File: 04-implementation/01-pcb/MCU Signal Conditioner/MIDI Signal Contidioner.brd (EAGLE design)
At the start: 78 x 31.5 mm, 26 parts, among them J2 ARDUINO-CONN-8X2, J3 ARDUINO-CONN-8X2, U4 24CS01, U6 MCP1700-SOT89, X1 SSW-107-02-S-D, X2 SSW-107-02-S-D, X3 SSW-107-02-S-D, X4 SSW-107-02-S-D, X5 MINI-USB-SHIELD-32005-201

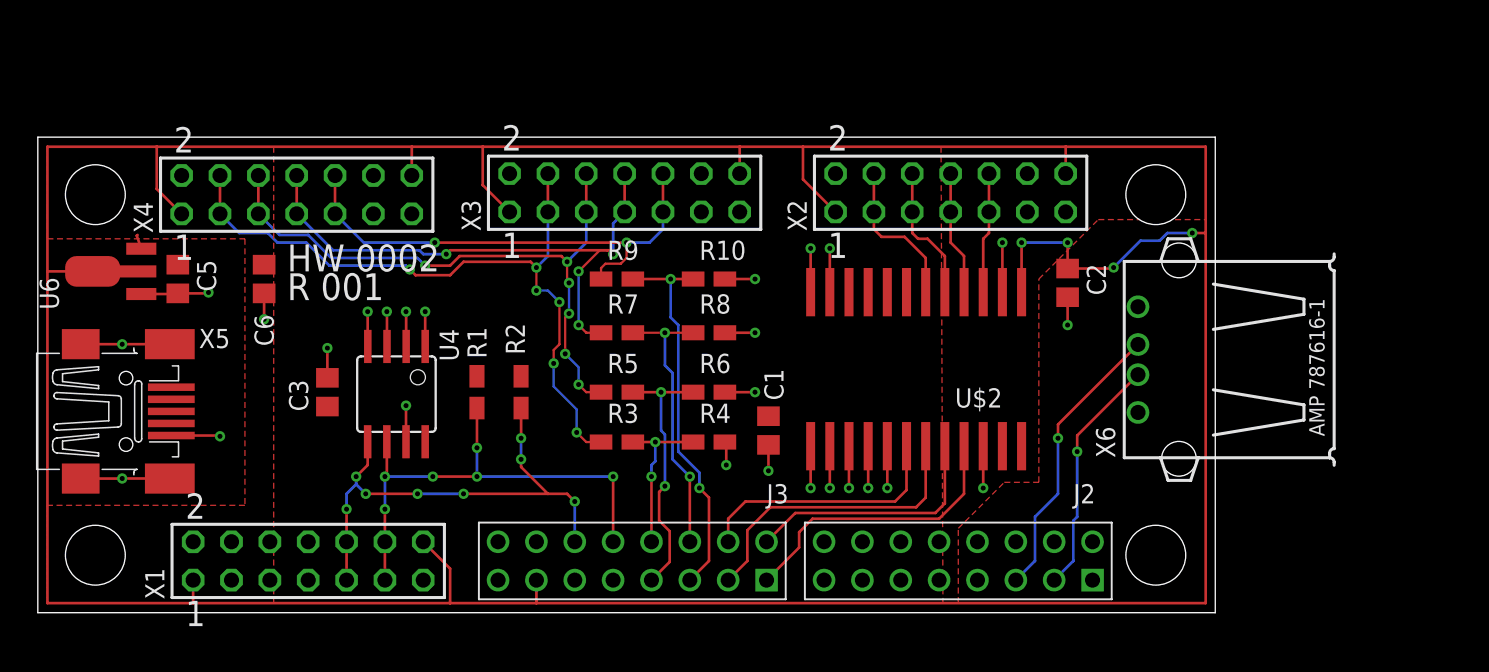
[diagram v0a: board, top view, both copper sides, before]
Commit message: Add files for PCB releases.
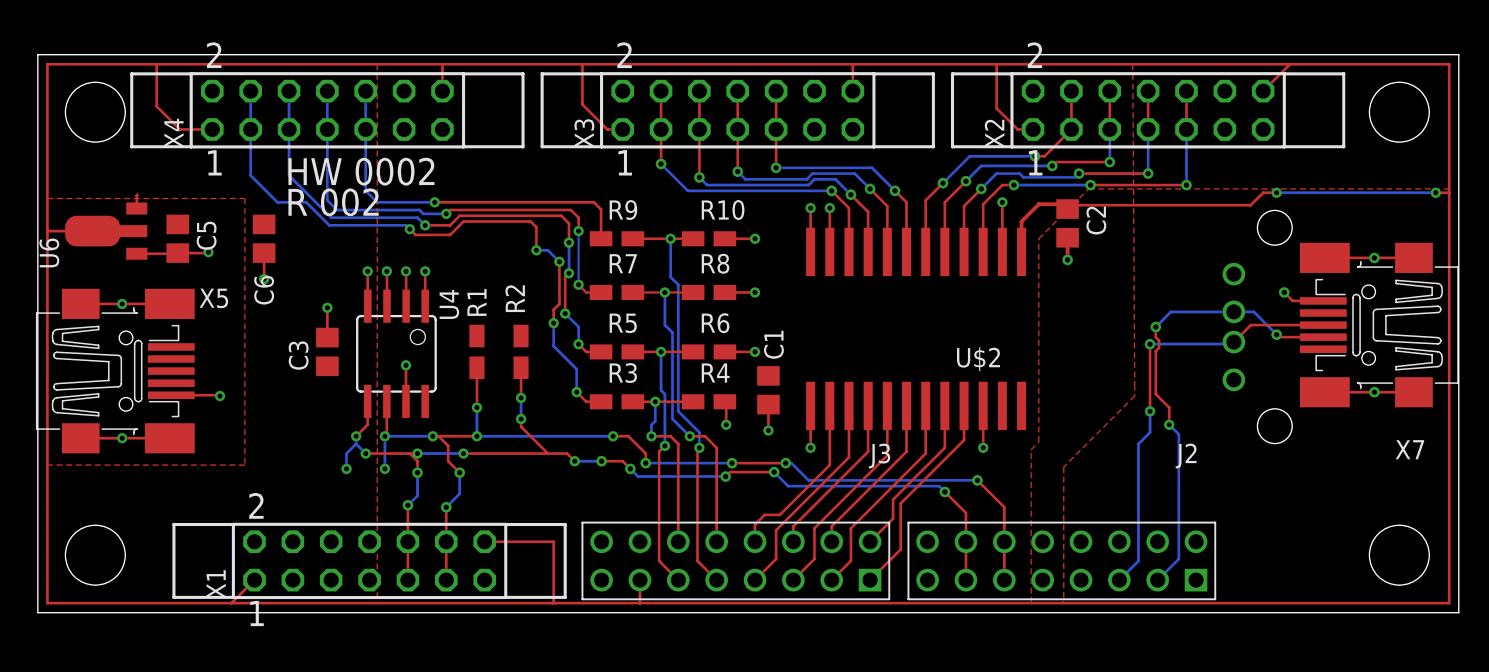
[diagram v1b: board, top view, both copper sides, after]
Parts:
- added X7: MINI-USB-SHIELD-32005-201, MIDI router parts:MINI-USB-32005-201
- U$2: device MIDI Signal Conditioner Parts:74LVC4245A-SO24 -> MIDI router parts:74LVC4245A-SO24
- U6: device MIDI Signal Conditioner Parts:MCP1700-SOT89 -> MIDI router parts:MCP1700-SOT89
- X1, X2, X3, X4: value SSW-107-02-S-D -> SSW-107-02-G-D; device con-samtec:SSW-107-02-S-D -> MIDI router parts:SSW-107-02-G-D
- X5: device MIDI Signal Conditioner Parts:MINI-USB-32005-201 -> MIDI router parts:MINI-USB-32005-201
- X6: device MIDI Signal Conditioner Parts:USB -> MIDI router parts:USB
- moved X2 14.2 mm to (73.5, 33.3)
- moved X3 9.27 mm to (46.4, 33.3)
- moved J2 6.86 mm to (76.7, 2.16)
- moved J3 6.86 mm to (55.1, 2.16)
- moved X6 6.71 mm to (92.2, 18.9), flipped to the bottom, turned to 270 degrees
- moved X4 5.95 mm to (19.2, 33.3)
- moved X1 4.06 mm to (22.0, 3.43)
- moved C2 3.94 mm to (68.2, 25.8)
- moved C5 2.67 mm to (9.27, 24.8)
- moved C6 2.67 mm to (15.0, 24.8)
- moved R10 2.67 mm to (44.5, 24.8)
- moved R9 2.67 mm to (38.4, 24.8)
- moved C1 2.67 mm to (48.4, 14.7)
- moved R3 2.67 mm to (38.4, 14.0)
- moved R4 2.67 mm to (44.5, 14.0)
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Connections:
- new net DT1: U$2.10, X3.3, X3.4
- new net DT1-3V: J3.P$8, U$2.14
- new net DT2: U$2.9, X3.5, X3.6
- new net DT2-3V: J3.P$7, U$2.15
- new net DT3: U$2.8, X3.7, X3.8
- new net DT3-3V: J3.P$6, U$2.16
- new net DT4: U$2.7, X3.10, X3.9
- new net DT4-3V: J3.P$5, U$2.17
- net DI1: no longer X3.3, X3.4
- net DI1-3V: now also J3.P$12; no longer J3.P$8
- net DI2: no longer X3.5, X3.6
- net DI2-3V: now also J3.P$11; no longer J3.P$7
- net DI3: no longer X3.7, X3.8
- net DI3-3V: now also J3.P$10; no longer J3.P$6
- net DI4: no longer X3.10, X3.9
- net DI4-3V: now also J3.P$9; no longer J3.P$5
- net GND: now also X7.5, X7.M1, X7.M2, X7.M3, X7.M4; no longer U$2.14, U$2.15, U$2.16, U$2.17
- net SCL: now also J2.P$11, J2.P$12; no longer J3.P$10
- net SDA: now also J2.P$13, J2.P$14; no longer J3.P$12
- net USB-D+: now also X7.3
- net USB-D-: now also X7.2
- net VBUS: now also X7.1
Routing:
- net +5V: track 263.7 -> 328.9 mm, vias 4 -> 2
- net SCL: track 33.2 -> 68.1 mm, vias 6 -> 12
- net SDA: track 33.8 -> 67.3 mm, vias 8 -> 15
- net DT1: track 0.00 -> 21.4 mm, vias 0 -> 2
- net DT2: track 0.00 -> 20.8 mm, vias 0 -> 2
- net DT3: track 0.00 -> 19.5 mm, vias 0 -> 2
- net DT4: track 0.00 -> 17.9 mm, vias 0 -> 2
- net DO4: track 8.01 -> 23.4 mm, vias 0 -> 3
- net USB-D-: track 15.9 -> 30.4 mm, vias 1 -> 3
- net DT4-3V: track 0.00 -> 14.1 mm
- net DT2-3V: track 0.00 -> 14.1 mm
- net DO3: track 8.22 -> 21.8 mm, vias 0 -> 3
- net DT1-3V: track 0.00 -> 11.6 mm
- net DT3-3V: track 0.00 -> 11.0 mm
- net DO2: track 9.12 -> 20.0 mm, vias 0 -> 3
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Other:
- board size 78 x 31.5 mm -> 94.1 x 37 mm
- board text added: "3. verify board-to-board connectors, etc. on checklist"
- board text added: "D+"
- board text added: "D-"
- board text added: "R 002"
- board text added: "V+"
- board text added: "V-"
- board text removed: "R 001"

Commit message: Add files for pushbutton PCB.
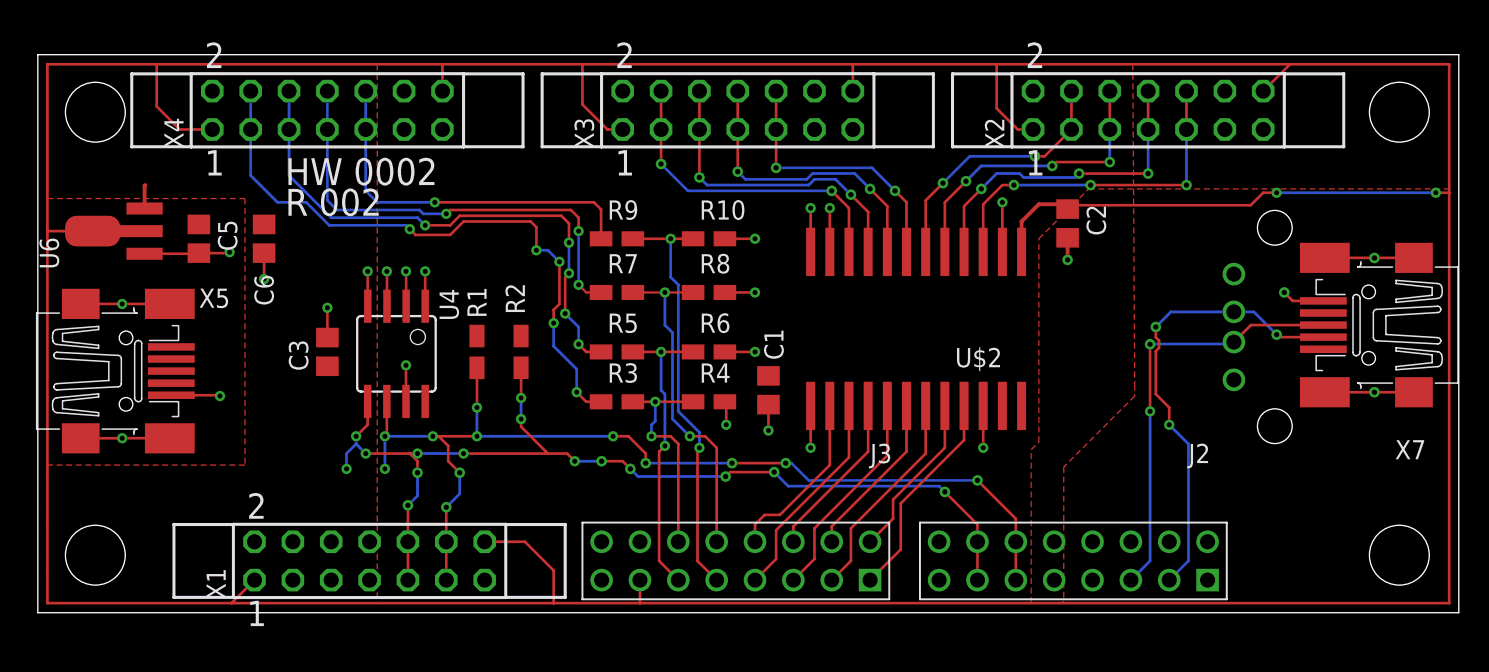
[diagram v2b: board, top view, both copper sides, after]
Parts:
- moved C5 1.40 mm to (10.7, 24.8)
- moved J2 0.76 mm to (77.5, 2.16)
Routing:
- net +5V: track 328.9 -> 327.8 mm
- net GND: track 75.2 -> 76.0 mm
- net +3V3: track 0.94 -> 1.57 mm
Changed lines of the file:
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@@
 </autorouter>
 <elements>
-<element name="J2" library="MIDI router MCU parts" package="ARDUINO-CONN-8X2" value="ARDUINO-CONN-8X2" x="76.708" y="2.159" smashed="yes" rot="R180">
-<attribute name="NAME" x="75.438" y="9.906" size="1.27" layer="25"/>
-<attribute name="VALUE" x="77.978" y="0.889" size="1.27" layer="27" rot="R180"/>
+<element name="J2" library="MIDI router MCU parts" package="ARDUINO-CONN-8X2" value="ARDUINO-CONN-8X2" x="77.47" y="2.159" smashed="yes" rot="R180">
+<attribute name="NAME" x="76.2" y="9.906" size="1.27" layer="25"/>
+<attribute name="VALUE" x="78.74" y="0.889" size="1.27" layer="27" rot="R180"/>
 </element>
 <element name="J3" library="MIDI router MCU parts" package="ARDUINO-CONN-8X2" value="ARDUINO-CONN-8X2" x="55.118" y="2.159" smashed="yes" rot="R180">
@@
 <attribute name="VALUE" x="8.9169" y="22.8679" size="1.27" layer="27" rot="R90"/>
 </element>
-<element name="C5" library="rcl" library_urn="urn:adsk.eagle:library:334" package="C0805" package3d_urn="urn:adsk.eagle:package:23617/2" value="1u" x="9.271" y="24.765" smashed="yes" rot="R270">
-<attribute name="NAME" x="10.541" y="26.035" size="1.27" layer="25" rot="R270"/>
-<attribute name="SPICEPREFIX" value="C" x="9.271" y="24.765" size="1.778" layer="27" rot="R270" display="off"/>
-<attribute name="VALUE" x="6.731" y="26.035" size="1.27" layer="27" rot="R270"/>
+<element name="C5" library="rcl" library_urn="urn:adsk.eagle:library:334" package="C0805" package3d_urn="urn:adsk.eagle:package:23617/2" value="1u" x="10.668" y="24.765" smashed="yes" rot="R270">
+<attribute name="NAME" x="11.938" y="26.035" size="1.27" layer="25" rot="R270"/>
+<attribute name="SPICEPREFIX" value="C" x="10.668" y="24.765" size="1.778" layer="27" rot="R270" display="off"/>
+<attribute name="VALUE" x="8.128" y="26.035" size="1.27" layer="27" rot="R270"/>
 </element>
 <element name="C6" library="rcl" library_urn="urn:adsk.eagle:library:334" package="C0805" package3d_urn="urn:adsk.eagle:package:23617/2" value="1u" x="14.986" y="24.765" smashed="yes" rot="R270">
@@
 <contactref element="J3" pad="P$13"/>
 <wire x1="39.878" y1="2.159" x2="39.878" y2="0.635" width="0.1778" layer="1"/>
-<wire x1="39.878" y1="0.635" x2="34.163" y2="0.635" width="0.1778" layer="1"/>
 <wire x1="12.827" y1="0.635" x2="0.635" y2="0.635" width="0.1778" layer="1"/>
 <wire x1="0.635" y1="0.635" x2="0.635" y2="25.273" width="0.1778" layer="1"/>
@@
 <wire x1="7.874" y1="33.528" x2="7.874" y2="36.322" width="0.1778" layer="1"/>
 <wire x1="14.351" y1="2.159" x2="12.827" y2="0.635" width="0.1778" layer="1"/>
-<wire x1="29.591" y1="4.699" x2="34.163" y2="4.699" width="0.1778" layer="1"/>
-<wire x1="34.163" y1="4.699" x2="34.163" y2="0.635" width="0.1778" layer="1"/>
 <wire x1="93.472" y1="36.322" x2="82.931" y2="36.322" width="0.1778" layer="1"/>
 <wire x1="81.153" y1="34.544" x2="82.931" y2="36.322" width="0.1778" layer="1"/>
@@
 <wire x1="66.294" y1="27.051" x2="67.945" y2="27.051" width="0.254" layer="1"/>
 <wire x1="67.945" y1="27.051" x2="68.232" y2="26.764" width="0.254" layer="1"/>
+<wire x1="39.878" y1="0.635" x2="34.163" y2="0.635" width="0.1778" layer="1"/>
 <wire x1="34.163" y1="0.635" x2="12.827" y2="0.635" width="0.1778" layer="1"/>
+<wire x1="29.591" y1="4.699" x2="32.258" y2="4.699" width="0.1778" layer="1"/>
+<wire x1="32.258" y1="4.699" x2="34.163" y2="2.794" width="0.1778" layer="1"/>
+<wire x1="34.163" y1="2.794" x2="34.163" y2="0.635" width="0.1778" layer="1"/>
 </signal>
 <signal name="GND">
@@
 <via x="5.588" y="20.447" extent="1-16" drill="0.3302"/>
 <wire x1="8.742" y1="20.452" x2="5.583" y2="20.452" width="0.1778" layer="1"/>
-<wire x1="6.553" y1="23.774" x2="9.23" y2="23.774" width="0.1778" layer="1"/>
-<wire x1="9.23" y1="23.774" x2="9.271" y2="23.815" width="0.1778" layer="1"/>
-<wire x1="9.271" y1="23.815" x2="11.242" y2="23.815" width="0.1778" layer="1"/>
-<wire x1="11.242" y1="23.815" x2="11.303" y2="23.876" width="0.1778" layer="1"/>
-<via x="11.303" y="23.876" extent="1-16" drill="0.3302"/>
+<wire x1="7.072" y1="23.774" x2="10.627" y2="23.774" width="0.1778" layer="1"/>
+<wire x1="10.627" y1="23.774" x2="10.668" y2="23.815" width="0.1778" layer="1"/>
+<wire x1="10.668" y1="23.815" x2="12.639" y2="23.815" width="0.1778" layer="1"/>
+<wire x1="12.639" y1="23.815" x2="12.7" y2="23.876" width="0.1778" layer="1"/>
+<via x="12.7" y="23.876" extent="1-16" drill="0.3302"/>
 <wire x1="8.842" y1="14.402" x2="12.014" y2="14.402" width="0.1778" layer="1"/>
 <wire x1="12.014" y1="14.402" x2="12.065" y2="14.351" width="0.1778" layer="1"/>
@@
 <contactref element="R1" pad="1"/>
 <contactref element="R2" pad="1"/>
-<wire x1="6.553" y1="26.772" x2="6.553" y2="27.635" width="0.1778" layer="1"/>
-<wire x1="6.553" y1="27.635" x2="6.604" y2="27.686" width="0.1778" layer="1"/>
 <contactref element="U$2" pad="24"/>
 <contactref element="U$2" pad="23"/>
 <contactref element="C1" pad="1"/>
+<wire x1="7.072" y1="26.772" x2="7.072" y2="28.281" width="0.254" layer="1"/>
+<wire x1="7.072" y1="28.281" x2="7.112" y2="28.321" width="0.254" layer="1"/>
 </signal>
 <signal name="SDA">
@@
 <contactref element="J2" pad="P$13"/>
 <contactref element="J2" pad="P$14"/>
-<wire x1="61.468" y1="2.159" x2="61.468" y2="4.699" width="0.1778" layer="1"/>
-<wire x1="61.468" y1="4.699" x2="61.468" y2="6.604" width="0.1778" layer="1"/>
-<wire x1="61.468" y1="6.604" x2="60.071" y2="8.001" width="0.1778" layer="1"/>
+<wire x1="62.23" y1="2.159" x2="62.23" y2="4.699" width="0.1778" layer="1"/>
+<wire x1="62.23" y1="4.699" x2="62.23" y2="5.842" width="0.1778" layer="1"/>
+<wire x1="62.23" y1="5.842" x2="60.071" y2="8.001" width="0.1778" layer="1"/>
 <via x="60.071" y="8.001" extent="1-16" drill="0.35"/>
 <wire x1="60.071" y1="8.001" x2="59.69" y2="8.382" width="0.1778" layer="16"/>
@@
 <contactref element="J2" pad="P$11"/>
 <contactref element="J2" pad="P$12"/>
-<wire x1="64.008" y1="2.159" x2="64.008" y2="4.699" width="0.1778" layer="1"/>
-<wire x1="64.008" y1="4.699" x2="64.008" y2="6.985" width="0.1778" layer="1"/>
-<wire x1="64.008" y1="6.985" x2="62.23" y2="8.763" width="0.1778" layer="1"/>
+<wire x1="64.77" y1="2.159" x2="64.77" y2="4.699" width="0.1778" layer="1"/>
+<wire x1="64.77" y1="4.699" x2="64.77" y2="6.223" width="0.1778" layer="1"/>
+<wire x1="64.77" y1="6.223" x2="62.23" y2="8.763" width="0.1778" layer="1"/>
 <via x="62.23" y="8.763" extent="1-16" drill="0.35"/>
 <wire x1="62.23" y1="8.763" x2="51.054" y2="8.763" width="0.1778" layer="16"/>
@@
 <contactref element="X6" pad="2"/>
 <via x="74.93" y="12.446" extent="1-16" drill="0.3302"/>
-<wire x1="74.168" y1="2.159" x2="75.565" y2="3.556" width="0.1778" layer="16"/>
-<wire x1="74.93" y1="12.446" x2="75.565" y2="11.811" width="0.1778" layer="16"/>
-<wire x1="75.565" y1="11.811" x2="75.565" y2="3.556" width="0.1778" layer="16"/>
+<wire x1="74.93" y1="2.159" x2="76.2" y2="3.429" width="0.1778" layer="16"/>
+<wire x1="74.93" y1="12.446" x2="76.2" y2="11.176" width="0.1778" layer="16"/>
+<wire x1="76.2" y1="11.176" x2="76.2" y2="3.429" width="0.1778" layer="16"/>
 <contactref element="X7" pad="2"/>
 <wire x1="74.93" y1="12.446" x2="74.93" y2="13.589" width="0.1778" layer="1"/>
@@
 <contactref element="X6" pad="3"/>
 <via x="73.66" y="13.335" extent="1-16" drill="0.3302"/>
-<wire x1="71.628" y1="2.159" x2="72.898" y2="3.429" width="0.1778" layer="16"/>
 <contactref element="X7" pad="3"/>
 <wire x1="73.66" y1="17.78" x2="73.66" y2="13.335" width="0.1778" layer="1"/>
@@
 <wire x1="85.138" y1="19.05" x2="80.3389" y2="19.05" width="0.1778" layer="1"/>
 <wire x1="80.3389" y1="19.05" x2="79.2119" y2="17.923" width="0.1778" layer="1"/>
-<wire x1="73.66" y1="11.938" x2="73.66" y2="13.335" width="0.1778" layer="16"/>
-<wire x1="72.898" y1="3.429" x2="72.898" y2="11.176" width="0.1778" layer="16"/>
-<wire x1="72.898" y1="11.176" x2="73.66" y2="11.938" width="0.1778" layer="16"/>
+<wire x1="73.66" y1="3.429" x2="72.39" y2="2.159" width="0.1778" layer="16"/>
+<wire x1="73.66" y1="13.335" x2="73.66" y2="3.429" width="0.1778" layer="16"/>
 </signal>
 <signal name="VBUS">
